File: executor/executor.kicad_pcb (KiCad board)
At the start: 4 copper layers, 58 x 58 mm, 134 parts, among them J1 XT30PW(2+2), Q1 WNM6006, Q2 WNM6006, Q3 WNM6006, Q4 WNM6006, Q5 WNM6006, Q6 WNM6006, U1 WD1601E, U2 DRV8323SRTAT, U3 GD32F303RETx, U4 TCAN4550RGYRQ1, U5 AS5047P-ATSM, U6 QMA7981, Y1 8M, Y2 40M

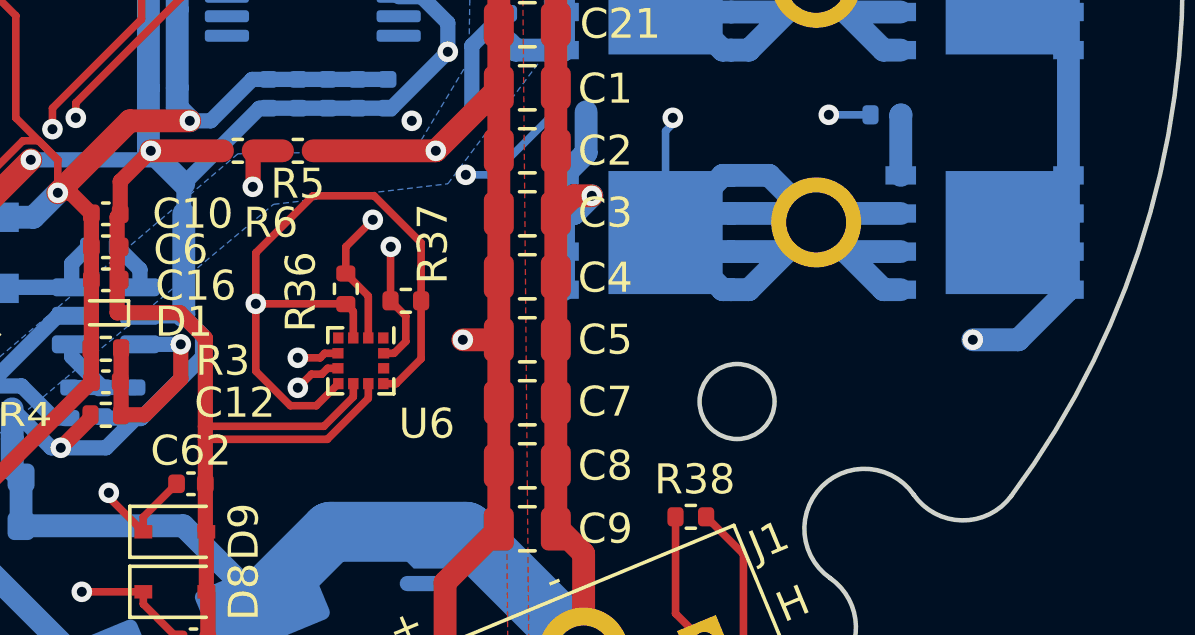
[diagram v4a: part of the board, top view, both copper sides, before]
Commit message: [New] Add comments to PCB board & Fix unconnected
1. Add date & signature to PCB board
2. Fix an unconnected wire

Signed-off-by: Homalozoa <nx.tardis@gmail.com>
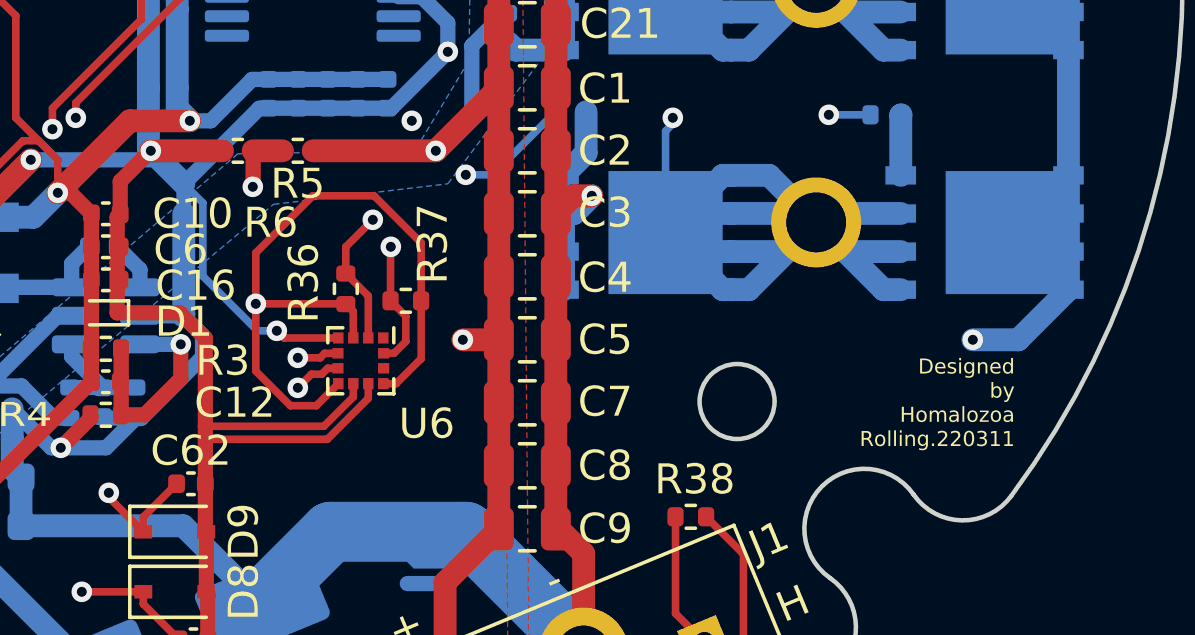
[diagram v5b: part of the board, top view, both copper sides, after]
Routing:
- net GND: track 281.6 -> 290.3 mm, vias 10 -> 11
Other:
- board text added: "Designed by Homalozoa Rolling.220311"
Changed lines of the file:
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@@
     (property "Sheetname" "")
     (attr smd)
-    (fp_text reference "R36" (at 0.1 1.5 90) (layer "F.SilkS")
+    (fp_text reference "R36" (at -0.2 1.4 90) (layer "F.SilkS")
       (effects (font (size 1 1) (thickness 0.15)))
     )
@@
   (gr_arc locked (start 57.755316 39.971998) (mid 56.895935 38.361297) (end 57.702474 36.723496) (layer "Edge.Cuts") (width 0.15))
   (gr_circle (center 75 59.985) (end 106 59.985) (layer "Margin") (width 0.1) (fill none))
+  (gr_text "Designed\nby\nHomalozoa\nRolling.220311" (at 98.4 74.185) (layer "F.SilkS")
+    (effects (font (size 0.5 0.5) (thickness 0.05)) (justify right))
+  )
+  (segment (start 75.85 72.0225) (end 74.0375 72.0225) (width 0.254) (layer "F.Cu") (net 1))
   (segment (start 69.6 65.785) (end 71.99 65.785) (width 0.762) (layer "F.Cu") (net 1))
   (segment (start 74.28 49.065) (end 74.28 49.485) (width 0.508) (layer "F.Cu") (net 1))
@@
   (segment (start 49.2 66.485) (end 49.2 67.761542) (width 0.508) (layer "F.Cu") (net 1))
   (segment (start 74 39.285) (end 76.24148 37.04352) (width 0.254) (layer "F.Cu") (net 1))
+  (segment (start 74.0375 72.0225) (end 73.8 71.785) (width 0.254) (layer "F.Cu") (net 1))
   (segment (start 57.9 63.981194) (end 58.514734 64.595928) (width 0.254) (layer "F.Cu") (net 1))
   (via (at 82.5 43.385) (size 0.6858) (drill 0.3302) (layers "F.Cu" "B.Cu") (net 1))
@@
   (via (at 49.2 66.485) (size 0.6858) (drill 0.3302) (layers "F.Cu" "B.Cu") (net 1))
   (via (at 79.5 62.485) (size 0.6858) (drill 0.3302) (layers "F.Cu" "B.Cu") (free) (net 1))
+  (via (at 73.8 71.785) (size 0.6858) (drill 0.3302) (layers "F.Cu" "B.Cu") (net 1))
   (via (at 65.6 66.085) (size 0.6858) (drill 0.3302) (layers "F.Cu" "B.Cu") (free) (net 1))
   (via (at 69.6 65.785) (size 0.6858) (drill 0.3302) (layers "F.Cu" "B.Cu") (net 1))
@@
   (segment (start 51.739376 66.145624) (end 51.4 66.485) (width 0.254) (layer "B.Cu") (net 1))
   (segment (start 67.52 57.685) (end 69.52 59.685) (width 0.508) (layer "B.Cu") (net 1))
+  (segment (start 71.33452 69.962974) (end 71.33452 67.51952) (width 0.254) (layer "B.Cu") (net 1))
   (segment (start 69.254594 53.939594) (end 69.254594 59.419594) (width 0.508) (layer "B.Cu") (net 1))
   (segment (start 73.4 52.585) (end 73.4 51.506178) (width 0.508) (layer "B.Cu") (net 1))
   (segment (start 65.6 66.085) (end 69.9 66.085) (width 0.508) (layer "B.Cu") (net 1))
+  (segment (start 73.156546 71.785) (end 71.33452 69.962974) (width 0.254) (layer "B.Cu") (net 1))
   (segment (start 79.5 62.485) (end 79.5 61.520443) (width 0.508) (layer "B.Cu") (net 1))
   (segment (start 73.520101 64.365) (end 73.22 64.365) (width 0.508) (layer "B.Cu") (net 1))
@@
   (segment (start 73.520101 64.365) (end 77.479899 64.365) (width 0.508) (layer "B.Cu") (net 1))
   (segment (start 48.5 58.085) (end 48.9 57.685) (width 0.508) (layer "B.Cu") (net 1))
+  (segment (start 71.33452 67.51952) (end 70.7 66.885) (width 0.254) (layer "B.Cu") (net 1))
   (segment (start 51.699689 61.284689) (end 51.699689 62.763511) (width 0.508) (layer "B.Cu") (net 1))
   (segment (start 48.9 57.685) (end 67.52 57.685) (width 0.508) (layer "B.Cu") (net 1))
@@
   (segment (start 48.5 58.085) (end 51.699689 61.284689) (width 0.508) (layer "B.Cu") (net 1))
   (segment (start 69.52 63.685) (end 69.52 65.705) (width 0.762) (layer "B.Cu") (net 1))
+  (segment (start 73.8 71.785) (end 73.156546 71.785) (width 0.254) (layer "B.Cu") (net 1))
   (segment (start 73.4 51.506178) (end 71.239411 49.345589) (width 0.508) (layer "B.Cu") (net 1))
   (segment (start 69.52 65.705) (end 69.6 65.785) (width 0.762) (layer "B.Cu") (net 1))
@@
     (connect_pads (clearance 0.508))
     (min_thickness 0.254) (filled_areas_thickness no)
-    (fill yes (thermal_gap 0.508) (thermal_bridge_width 0.508))
+    (fill (thermal_gap 0.508) (thermal_bridge_width 0.508))
     (polygon
       (pts
@@
     (connect_pads (clearance 0.508))
     (min_thickness 0.254) (filled_areas_thickness no)
-    (fill yes (thermal_gap 0.508) (thermal_bridge_width 0.508))
+    (fill (thermal_gap 0.508) (thermal_bridge_width 0.508))
     (polygon
       (pts
@@
     (polygon
       (pts
+        (xy 77.9 74.085)
+        (xy 75.3 74.085)
+        (xy 75.3 71.485)
+        (xy 77.9 71.485)
+      )
+    )
+  )
+  (zone (net 0) (net_name "") (layers "F.Cu" "In1.Cu" "In2.Cu" "B.Cu") (hatch edge 0.508)
+    (connect_pads (clearance 0))
+    (min_thickness 0.254)
+    (keepout (tracks allowed) (vias allowed) (pads allowed ) (copperpour not_allowed) (footprints allowed))
+    (fill (thermal_gap 0.508) (thermal_bridge_width 0.508))
+    (polygon
+      (pts
         (xy 67.2 49.485)
         (xy 64.5 52.185)
@@
     (connect_pads (clearance 0.508))
     (min_thickness 0.254) (filled_areas_thickness no)
-    (fill yes (thermal_gap 0.508) (thermal_bridge_width 0.508) (smoothing fillet))
+    (fill (thermal_gap 0.508) (thermal_bridge_width 0.508) (smoothing fillet))
     (polygon
       (pts
@@
     (connect_pads (clearance 0.508))
     (min_thickness 0.254) (filled_areas_thickness no)
-    (fill yes (thermal_gap 0.508) (thermal_bridge_width 0.508))
+    (fill (thermal_gap 0.508) (thermal_bridge_width 0.508))
     (polygon
       (pts
@@
     (connect_pads (clearance 0.508))
     (min_thickness 0.254) (filled_areas_thickness no)
-    (fill yes (thermal_gap 0.508) (thermal_bridge_width 0.508))
+    (fill (thermal_gap 0.508) (thermal_bridge_width 0.508))
     (polygon
       (pts
@@
     (connect_pads (clearance 0.508))
     (min_thickness 0.254) (filled_areas_thickness no)
-    (fill yes (thermal_gap 0.508) (thermal_bridge_width 0.508))
+    (fill (thermal_gap 0.508) (thermal_bridge_width 0.508))
     (polygon
       (pts

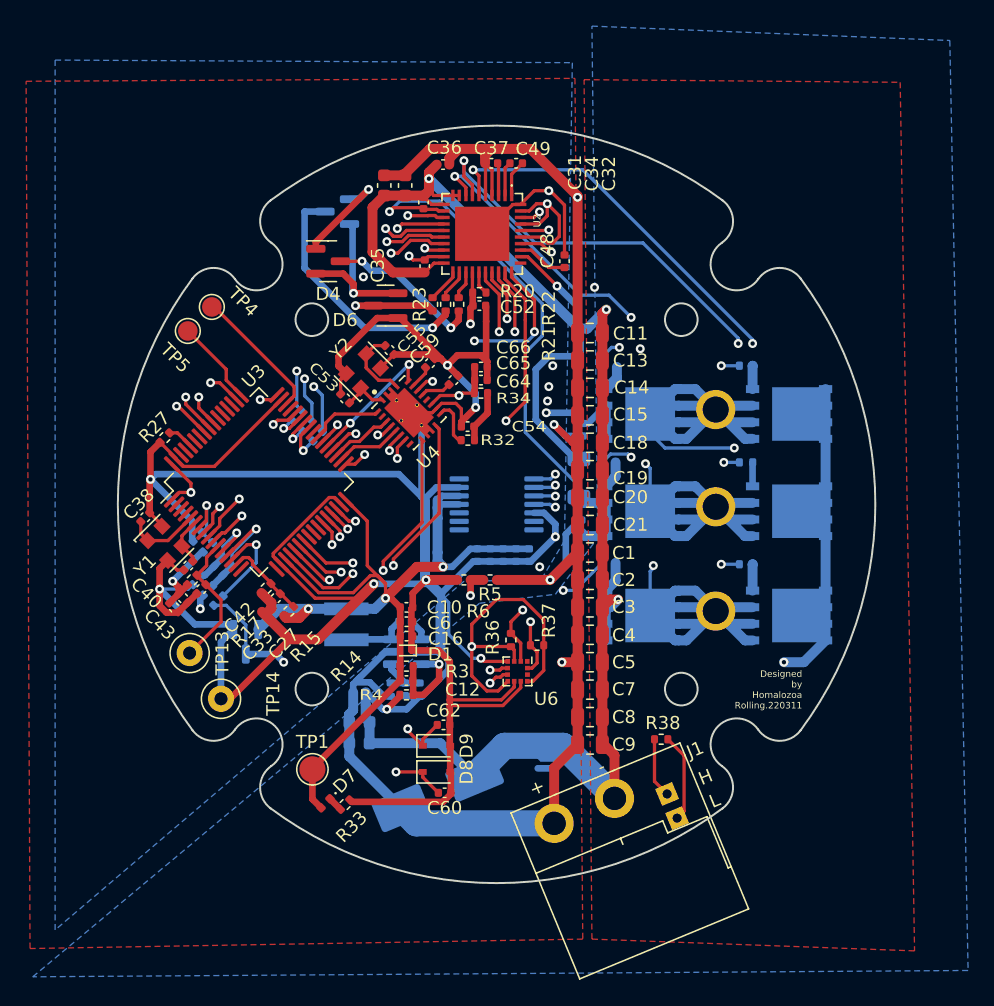
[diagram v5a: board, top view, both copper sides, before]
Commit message: [Modify] Change footprints for manufature
Signed-off-by: Homalozoa <nx.tardis@gmail.com>
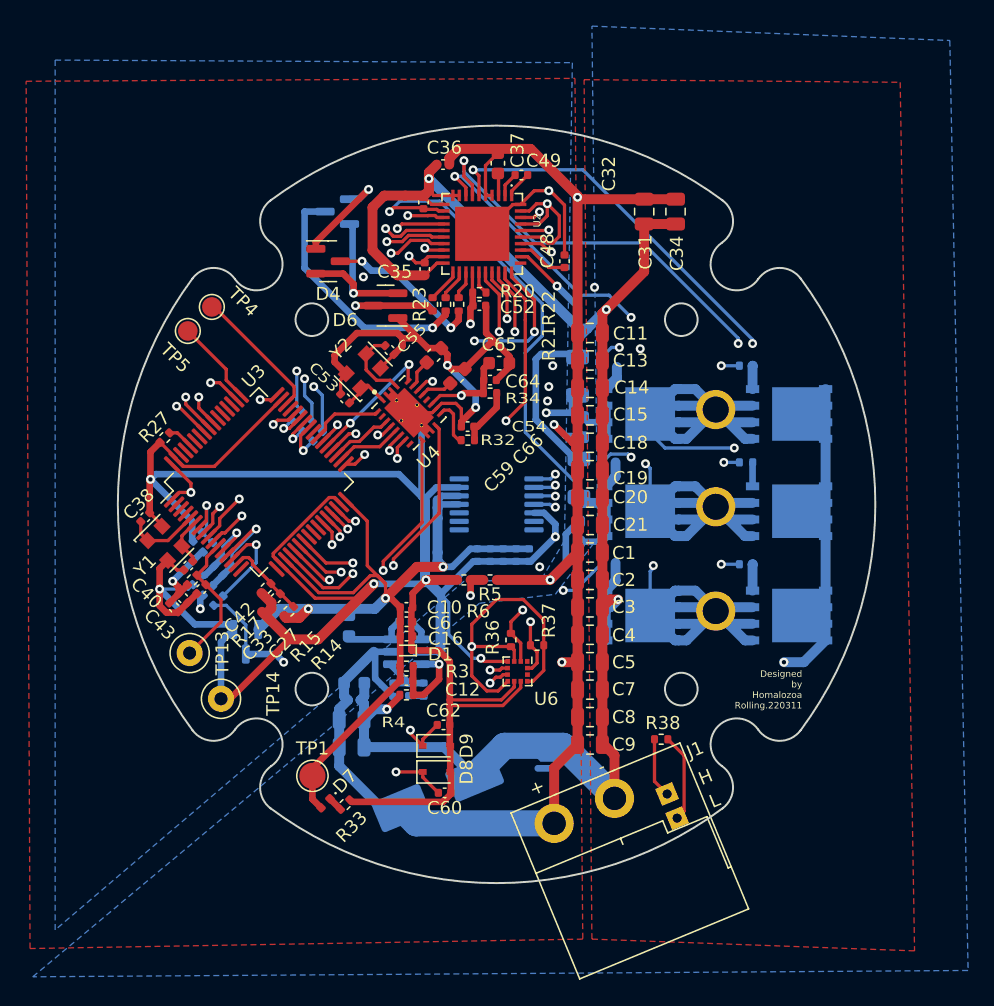
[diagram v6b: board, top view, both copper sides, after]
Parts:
- added R16: 0.001R, Resistor_SMD:R_1206_3216Metric, B.Cu at (81.2, 50.2)
- C10, C6: value 10uF, 10%, 50V -> 10uF, 20%, 6.3V
- C16: value 100nF, 10%, 50V -> 100nF, 10%, 10V
- C17, C25, C29, C37, C65, C66: footprint Capacitor_SMD:C_0402_1005Metric -> Capacitor_SMD:C_0603_1608Metric
- C26, C28, C31, C34: footprint Capacitor_SMD:C_0603_1608Metric -> Capacitor_SMD:C_0805_2012Metric
- C38, C42: value 10pF, 10%, 10V -> 20pF, 10%, 10V
- C59: value 300nF, 10%, 50V -> 470nF, 10%, 50V; footprint Capacitor_SMD:C_0402_1005Metric -> Capacitor_SMD:C_0603_1608Metric
- L1: footprint Inductor_SMD:L_Coilcraft_XxL4040 -> Inductor_SMD:L_0603_1608Metric
- R33: value 10k, 5% -> 330R, 5%
- moved C34 20.8 mm to (88.7, 37.6)
- moved C31 20.0 mm to (86.3, 37.6)
- moved C65 1.43 mm to (75.2, 49.2)
- moved C49 0.98 mm to (76.9, 34.8)
- moved C17 0.81 mm to (64.1, 73.7)
- moved C64 0.70 mm to (74.5, 50.5)
- moved R34 0.70 mm to (74.5, 51.5)
- moved C28 0.67 mm to (63.9, 78.6)
- moved C59 0.67 mm to (70.2, 48.6)
- moved C26 0.63 mm to (63.9, 76.5)
- moved C30 0.57 mm to (64.1, 75.0)
- moved C37 0.50 mm to (75.1, 33.9), turned to -90 degrees
- moved TP1 0.50 mm to (60.9, 80.8)
- moved C25 0.45 mm to (81.3, 62.1)
- moved C66 0.42 mm to (72.0, 50.2)
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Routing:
- net GNDA: track 149.7 -> 154.3 mm
- net +24V: track 198.6 -> 201.0 mm
- net ICP: track 37.8 -> 39.0 mm
- net GND: track 290.3 -> 291.4 mm
- net VCP: track 2.40 -> 1.64 mm
- net Net-(C49-Pad2): track 2.81 -> 2.07 mm
- net Net-(C49-Pad1): track 2.62 -> 1.88 mm

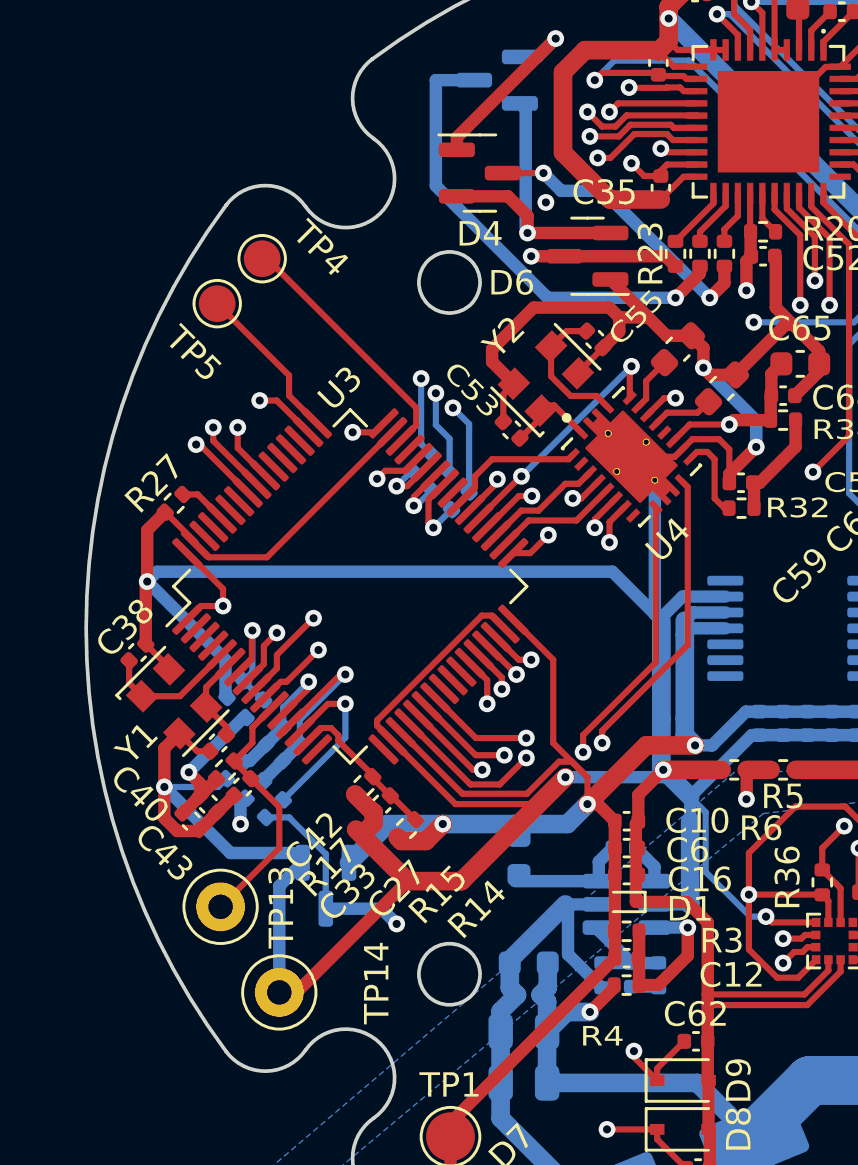
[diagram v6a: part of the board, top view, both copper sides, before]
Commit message: [Fix] Fix tcan4550 spi wrong connection
Signed-off-by: Homalozoa <nx.tardis@gmail.com>
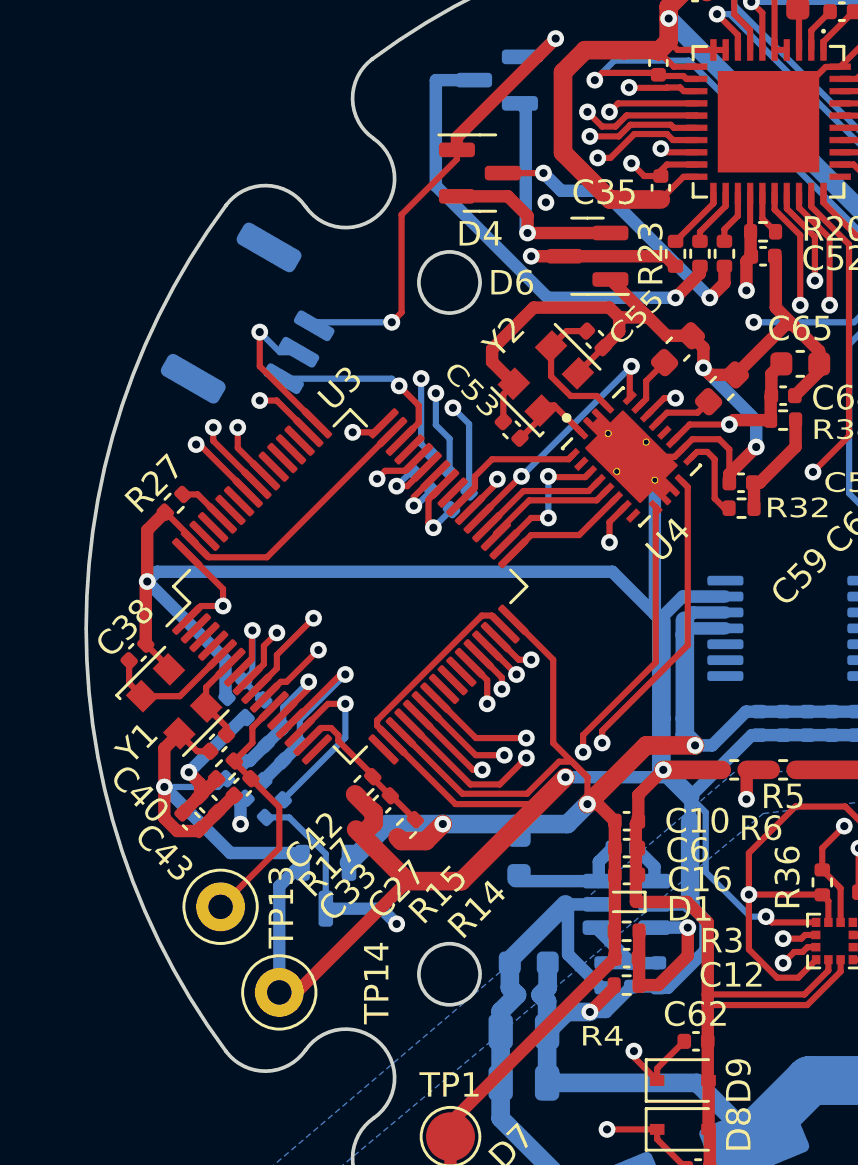
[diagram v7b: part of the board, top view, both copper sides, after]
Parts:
- removed TP4: SWDIO, TestPoint:TestPoint_Pad_D1.5mm
- removed TP5: SWCLK, TestPoint:TestPoint_Pad_D1.5mm
- added J2: gh1.25, 3p, Connector_JST:JST_GH_SM03B-GHS-TB_1x03-1MP_P1.25mm_Horizontal, B.Cu at (53.1, 47.8)
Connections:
- U3 pad 33: TCAN_SDI -> TCAN_SCS
- U3 pad 34: TCAN_SDO -> TCAN_SCK
- U3 pad 35: TCAN_SCK -> TCAN_SDO
- U3 pad 36: TCAN_SCS -> TCAN_SDI
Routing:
- net GND: track 291.4 -> 302.8 mm, vias 11 -> 12
- net GNDA: track 154.3 -> 161.1 mm
- net SWDIO: track 10.4 -> 7.72 mm, vias 0 -> 1
- net TCAN_SCS: track 7.00 -> 5.13 mm, vias 2 -> 0
- net TCAN_SCK: track 4.92 -> 5.74 mm, vias 0 -> 2
- net TCAN_SDI: track 5.01 -> 5.33 mm, vias 2 -> 0
- net SWCLK: track 6.59 -> 6.65 mm, vias 0 -> 1
